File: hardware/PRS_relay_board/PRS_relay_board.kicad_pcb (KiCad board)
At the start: 2 copper layers, 28 parts, among them J1 691317410002, J2 691317410002, J3 691317410002, J4 691317410002, J5 UJ2-BH-2-TH, J6 530470610, J7 530470410, K1 T9AS1D12-5, K2 T9AS1D12-5, K3 T9AS1D12-5, K4 T9AS1D12-5, Q1 PMV37ENEA, Q2 PMV37ENEA, Q3 PMV37ENEA, Q4 PMV37ENEA

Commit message: Commit
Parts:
- removed J5: UJ2-BH-2-TH, UJ2-BH-2-TH:CUI_UJ2-BH-2-TH
- removed J6: 530470610, 530470610:MOLEX_530470610
- removed J7: 530470410, 530470410:MOLEX_530470410
- added C1: 100n, Capacitor_SMD:C_0603_1608Metric_Pad1.08x0.95mm_HandSolder, F.Cu at (234.0, -70.7)
- added C10: 100n, Capacitor_SMD:C_0603_1608Metric_Pad1.08x0.95mm_HandSolder, F.Cu at (224.9, -64.4)
- added C11: 100n, Capacitor_SMD:C_0603_1608Metric_Pad1.08x0.95mm_HandSolder, F.Cu at (229.7, -68.4)
- added C12: 100n, Capacitor_SMD:C_0603_1608Metric_Pad1.08x0.95mm_HandSolder, F.Cu at (223.7, -61.9)
- added C13: 10u, Capacitor_SMD:C_0805_2012Metric_Pad1.18x1.45mm_HandSolder, F.Cu at (131.0, 151.0)
- added C14: 100n, Capacitor_SMD:C_0603_1608Metric_Pad1.08x0.95mm_HandSolder, F.Cu at (241.7, -78.2)
- added C15: 100n, Capacitor_SMD:C_0603_1608Metric_Pad1.08x0.95mm_HandSolder, F.Cu at (219.4, -56.9)
- added C16: 100n, Capacitor_SMD:C_0603_1608Metric_Pad1.08x0.95mm_HandSolder, F.Cu at (237.1, -73.2)
- added C17: 1u, Capacitor_SMD:C_0603_1608Metric_Pad1.08x0.95mm_HandSolder, F.Cu at (229.7, -65.9)
- added C18: 100n, Capacitor_SMD:C_0603_1608Metric_Pad1.08x0.95mm_HandSolder, F.Cu at (246.5, -81.2)
- added C2: 100n, Capacitor_SMD:C_0603_1608Metric_Pad1.08x0.95mm_HandSolder, F.Cu at (248.9, -76.2)
- added C3: 10u, Capacitor_SMD:C_0805_2012Metric_Pad1.18x1.45mm_HandSolder, F.Cu at (237.6, -81.0)
- added C4: 100n, Capacitor_SMD:C_0603_1608Metric_Pad1.08x0.95mm_HandSolder, F.Cu at (231.5, -75.7)
- added C5: 100n, Capacitor_SMD:C_0603_1608Metric_Pad1.08x0.95mm_HandSolder, F.Cu at (237.4, -78.2)
- added C6: 100n, Capacitor_SMD:C_0603_1608Metric_Pad1.08x0.95mm_HandSolder, F.Cu at (219.4, -61.9)
- added C7: 100n, Capacitor_SMD:C_0603_1608Metric_Pad1.08x0.95mm_HandSolder, F.Cu at (232.8, -73.2)
- added C8: 100n, Capacitor_SMD:C_0603_1608Metric_Pad1.08x0.95mm_HandSolder, F.Cu at (242.2, -81.2)
- added C9: 100n, Capacitor_SMD:C_0603_1608Metric_Pad1.08x0.95mm_HandSolder, F.Cu at (235.8, -75.7)
- added FB1: Ferrite_Bead, Resistor_SMD:R_0603_1608Metric_Pad0.98x0.95mm_HandSolder, F.Cu at (223.7, -59.4)
- added H1: MountingHole, MountingHole:MountingHole_3.2mm_M3_DIN965, F.Cu at (78.0, 37.0)
- added H2: MountingHole, MountingHole:MountingHole_3.2mm_M3_DIN965, F.Cu at (151.0, 38.0)
- added IC1: USBLC6-4SC6, USBLC6-4SC6:SOT95P280X145-6N, F.Cu at (174.0, 39.0)
- added IC2: 74LVC125AD,118, 74LVC125AD,118:SOIC127P600X175-14N, F.Cu at (172.0, 129.0)
- added LED1: 553-0122F, 553-0122:5530122F, F.Cu at (55.0, 175.5)
- added LED2: 553-0122F, 553-0122:5530122F, F.Cu at (92.5, 175.5)
- added LED3: 553-0122F, 553-0122:5530122F, F.Cu at (130.0, 175.5)
- added LED4: 553-0122F, 553-0122:5530122F, F.Cu at (167.5, 175.5)
- added R10: 100k, Resistor_SMD:R_0603_1608Metric_Pad0.98x0.95mm_HandSolder, F.Cu at (232.4, -60.6)
- added R11: 100k, Resistor_SMD:R_0603_1608Metric_Pad0.98x0.95mm_HandSolder, F.Cu at (242.7, -70.7)
- added R12: 1k, Resistor_SMD:R_0603_1608Metric_Pad0.98x0.95mm_HandSolder, F.Cu at (228.1, -56.9)
- added R13: 1k, Resistor_SMD:R_0603_1608Metric_Pad0.98x0.95mm_HandSolder, F.Cu at (238.4, -68.2)
- added R14: 10k, Resistor_SMD:R_0603_1608Metric_Pad0.98x0.95mm_HandSolder, F.Cu at (245.5, -63.2)
- added R15: 10k, Resistor_SMD:R_0603_1608Metric_Pad0.98x0.95mm_HandSolder, F.Cu at (244.5, -75.7)
- added R16: 1k, Resistor_SMD:R_0603_1608Metric_Pad0.98x0.95mm_HandSolder, F.Cu at (228.1, -59.4)
- added R17: 1k, Resistor_SMD:R_0603_1608Metric_Pad0.98x0.95mm_HandSolder, F.Cu at (234.0, -65.7)
- added R18: 10k, Resistor_SMD:R_0603_1608Metric_Pad0.98x0.95mm_HandSolder, F.Cu at (241.5, -73.2)
- added R19: 10k, Resistor_SMD:R_0603_1608Metric_Pad0.98x0.95mm_HandSolder, F.Cu at (223.7, -56.9)
- added R20: 100R, Resistor_SMD:R_0603_1608Metric_Pad0.98x0.95mm_HandSolder, F.Cu at (238.4, -70.7)
- added R21: 100R, Resistor_SMD:R_0603_1608Metric_Pad0.98x0.95mm_HandSolder, F.Cu at (246.1, -78.7)
- added R22: 100R, Resistor_SMD:R_0603_1608Metric_Pad0.98x0.95mm_HandSolder, F.Cu at (234.0, -68.2)
- added R23: 100R, Resistor_SMD:R_0603_1608Metric_Pad0.98x0.95mm_HandSolder, F.Cu at (232.4, -63.1)
- added R24: 10k, Resistor_SMD:R_0603_1608Metric_Pad0.98x0.95mm_HandSolder, F.Cu at (236.8, -63.1)
- added R25: 1k, Resistor_SMD:R_0603_1608Metric_Pad0.98x0.95mm_HandSolder, F.Cu at (242.7, -68.2)
- added R26: 1k, Resistor_SMD:R_0603_1608Metric_Pad0.98x0.95mm_HandSolder, F.Cu at (232.4, -58.1)
- added R27: 10k, Resistor_SMD:R_0603_1608Metric_Pad0.98x0.95mm_HandSolder, F.Cu at (247.1, -70.7)
- added R28: 10k, Resistor_SMD:R_0603_1608Metric_Pad0.98x0.95mm_HandSolder, F.Cu at (236.8, -60.6)
- added R29: 330R, Resistor_SMD:R_0603_1608Metric_Pad0.98x0.95mm_HandSolder, F.Cu at (232.4, -55.6)
- added R30: 330R, Resistor_SMD:R_0603_1608Metric_Pad0.98x0.95mm_HandSolder, F.Cu at (242.7, -65.7)
- added R31: 330R, Resistor_SMD:R_0603_1608Metric_Pad0.98x0.95mm_HandSolder, F.Cu at (100.0, 172.5)
- added R32: 330R, Resistor_SMD:R_0603_1608Metric_Pad0.98x0.95mm_HandSolder, F.Cu at (100.0, 175.0)
- added R33: 330R, Resistor_SMD:R_0603_1608Metric_Pad0.98x0.95mm_HandSolder, F.Cu at (145.0, 207.5)
- added R34: 330R, Resistor_SMD:R_0603_1608Metric_Pad0.98x0.95mm_HandSolder, F.Cu at (145.0, 210.0)
- added R35: 330R, Resistor_SMD:R_0603_1608Metric_Pad0.98x0.95mm_HandSolder, F.Cu at (149.3, 207.5)
- added R36: 330R, Resistor_SMD:R_0603_1608Metric_Pad0.98x0.95mm_HandSolder, F.Cu at (149.3, 210.0)
- added R5: 1k, Resistor_SMD:R_0603_1608Metric_Pad0.98x0.95mm_HandSolder, F.Cu at (240.2, -75.7)
- added R6: 1k, Resistor_SMD:R_0603_1608Metric_Pad0.98x0.95mm_HandSolder, F.Cu at (228.1, -61.9)
- added R7: 10k, Resistor_SMD:R_0603_1608Metric_Pad0.98x0.95mm_HandSolder, F.Cu at (219.4, -59.4)
- added R8: 10k, Resistor_SMD:R_0603_1608Metric_Pad0.98x0.95mm_HandSolder, F.Cu at (238.4, -65.7)
- added R9: 100k, Resistor_SMD:R_0603_1608Metric_Pad0.98x0.95mm_HandSolder, F.Cu at (245.8, -73.2)
- added S1: 100SP1T2B4M7RE, 100SP1T2B4M7RE:100SP1T2B4M7RE, F.Cu at (35.0, 165.0)
- added S2: 100SP1T2B4M7RE, 100SP1T2B4M7RE:100SP1T2B4M7RE, F.Cu at (47.5, 165.0)
- added S3: 100SP1T2B4M7RE, 100SP1T2B4M7RE:100SP1T2B4M7RE, F.Cu at (72.5, 165.0)
- added S4: 100SP1T2B4M7RE, 100SP1T2B4M7RE:100SP1T2B4M7RE, F.Cu at (85.0, 165.0)
- added S5: 100SP1T2B4M7RE, 100SP1T2B4M7RE:100SP1T2B4M7RE, F.Cu at (110.0, 165.0)
- added S6: 100SP1T2B4M7RE, 100SP1T2B4M7RE:100SP1T2B4M7RE, F.Cu at (122.5, 165.0)
- added S7: 100SP1T2B4M7RE, 100SP1T2B4M7RE:100SP1T2B4M7RE, F.Cu at (147.5, 165.0)
- added S8: 100SP1T2B4M7RE, 100SP1T2B4M7RE:100SP1T2B4M7RE, F.Cu at (160.0, 165.0)
- added U1: MCP1825S-3302E/DB, Package_TO_SOT_SMD:SOT-223-3_TabPin2, F.Cu at (112.0, 145.0)
- added U2: STM32L052K6Tx, Package_QFP:LQFP-32_7x7mm_P0.8mm, F.Cu at (130.0, 141.0)
- J1, J2: value 691317410002 -> 691313410004; footprint 691317410002:691317410002 -> 691313410004:691313410004
- J3: value 691317410002 -> UJ2-BH-2-TH; footprint 691317410002:691317410002 -> UJ2-BH-2-TH:CUI_UJ2-BH-2-TH
- J4: value 691317410002 -> FTSH-105-01-F-DV-K-P; footprint 691317410002:691317410002 -> FTSH-105-01-F-DV-K:FTSH-105-XX-YYY-DV-K-P
- moved J4 113.6 mm to (155.0, 141.0), turned to 0 degrees
- moved D7 98.0 mm to (118.7, 101.6), turned to 270 degrees
- moved K3 90.4 mm to (91.8, 59.3), turned to 90 degrees
- moved D8 89.2 mm to (118.7, 94.0), turned to 270 degrees
- moved K4 87.1 mm to (130.2, 99.2), turned to 270 degrees
- moved D3 84.5 mm to (103.3, 56.9), turned to 90 degrees
- moved Q4 82.2 mm to (118.7, 87.7), turned to 270 degrees
- moved R4 78.2 mm to (118.7, 83.8), turned to 180 degrees
- moved D4 74.9 mm to (103.3, 64.7), turned to 90 degrees
- moved PS1 69.5 mm to (50.0, 119.0)
- moved Q3 67.7 mm to (103.3, 70.8), turned to 90 degrees
- moved R3 63.4 mm to (103.3, 74.6), turned to 0 degrees
- moved J1 53.4 mm to (65.0, 28.0), turned to 0 degrees
- moved D5 36.5 mm to (118.7, 70.7), turned to 270 degrees
- moved K1 35.4 mm to (91.8, 90.3), turned to 90 degrees
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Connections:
- J1 pad 1: Net-(J1-Pad1) -> /RELAY1_COM
- J1 pad 2: Net-(J1-Pad2) -> /RELAY1_NO
- J2 pad 1: Net-(J2-Pad1) -> /RELAY3_COM
- J2 pad 2: Net-(J2-Pad2) -> /RELAY3_NO
- J4 pad 1: Net-(J4-Pad1) -> +3V3
- J4 pad 2: Net-(J4-Pad2) -> /Sheet6168966E/SWDIO
- K1 pad 3: Net-(J1-Pad2) -> /RELAY1_COM
- K1 pad 4: Net-(J1-Pad1) -> /RELAY1_NO
- K2 pad 3: Net-(J2-Pad2) -> /RELAY3_COM
- K2 pad 4: Net-(J2-Pad1) -> /RELAY3_NO
- K3 pad 3: Net-(J3-Pad2) -> /RELAY2_COM
- K3 pad 4: Net-(J3-Pad1) -> /RELAY2_NO
- K4 pad 3: Net-(J4-Pad2) -> /RELAY4_COM
- K4 pad 4: Net-(J4-Pad1) -> /RELAY4_NO
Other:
- board outline added: 160 x 160 mm

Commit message: Commit
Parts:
- removed U1: MCP1825S-3302E/DB, Package_TO_SOT_SMD:SOT-223-3_TabPin2
- added C19: 100n, Capacitor_SMD:C_0603_1608Metric_Pad1.08x0.95mm_HandSolder, F.Cu at (233.2, 138.3)
- added D9: MMBD7000HC, Package_TO_SOT_SMD:SOT-23_Handsoldering, F.Cu at (161.0, 129.0)
- added H3: MountingHole, MountingHole:MountingHole_3.2mm_M3_DIN965, F.Cu at (65.0, 180.0)
- added H4: MountingHole, MountingHole:MountingHole_3.2mm_M3_DIN965, F.Cu at (215.0, 180.0)
- added IC3: STCN75, STCN75:SOP65P490X110-8N, F.Cu at (145.0, 135.0)
- added IC4: UA78M33CKVURG3, UA78M33CKVURG3:TPS7A6533QKVURQ1, F.Cu at (139.0, 126.0)
- added J5: 10-32-1031, 10-32-1031:SHDR3W114P0X508_1X3_1416X1140X1425P, F.Cu at (68.0, 129.0)
- added Q5: BC848, Package_TO_SOT_SMD:SOT-23_Handsoldering, F.Cu at (163.0, 118.0)
- added Q6: PMV37ENEA, Package_TO_SOT_SMD:SOT-23_Handsoldering, F.Cu at (167.4, 129.0)
- added R37: R, Resistor_SMD:R_0603_1608Metric_Pad0.98x0.95mm_HandSolder, F.Cu at (237.6, 138.3)
- added R38: R, Resistor_SMD:R_0603_1608Metric_Pad0.98x0.95mm_HandSolder, F.Cu at (201.4, 146.7)
- added R39: 100R, Resistor_SMD:R_0603_1608Metric_Pad0.98x0.95mm_HandSolder, F.Cu at (196.6, 129.7)
- added R40: 10k, Resistor_SMD:R_0603_1608Metric_Pad0.98x0.95mm_HandSolder, F.Cu at (168.4, 117.0)
- added R41: 1k, Resistor_SMD:R_0603_1608Metric_Pad0.98x0.95mm_HandSolder, F.Cu at (168.4, 119.5)
- added R42: 10k, Resistor_SMD:R_0603_1608Metric_Pad0.98x0.95mm_HandSolder, F.Cu at (159.9, 132.5)
- added R43: R, Resistor_SMD:R_0603_1608Metric_Pad0.98x0.95mm_HandSolder, F.Cu at (211.0, 81.0)
- added R44: R, Resistor_SMD:R_0603_1608Metric_Pad0.98x0.95mm_HandSolder, F.Cu at (211.0, 83.5)
- C3: value 10u -> 330n; footprint Capacitor_SMD:C_0805_2012Metric_Pad1.18x1.45mm_HandSolder -> Capacitor_SMD:C_0603_1608Metric_Pad1.08x0.95mm_HandSolder
- IC1: value USBLC6-4SC6 -> USBLC6-2SC6
- K1, K2, K3, K4: value T9AS1D12-5 -> 1-1393210-3; footprint T9AS1D12-5:T9AS1D125 -> T9AS1D12-12:TE_1-1393210-3
- PS1: value RAC10-05SK_277 -> RAC10-12SK_277; footprint RAC10-05SK_277:RAC1005SK277 -> RAC10-12SK_277:RAC10-12SK_277
- R9: value 100k -> R
- moved R5 290.4 mm to (78.0, 165.2), turned to 180 degrees
- moved C2 287.4 mm to (90.6, 163.6), turned to 180 degrees
- moved R30 281.8 mm to (93.0, 173.0), turned to 90 degrees
- moved C1 281.5 mm to (78.0, 163.6), turned to 180 degrees
- moved R8 275.5 mm to (90.6, 166.8)
- moved R15 269.9 mm to (126.0, 166.8)
- moved R7 266.7 mm to (78.0, 166.8)
- moved R29 266.4 mm to (95.6, 173.0), turned to 90 degrees
- moved R6 265.5 mm to (90.6, 165.2), turned to 180 degrees
- moved R14 265.1 mm to (113.6, 166.8)
- moved C7 259.8 mm to (126.0, 163.6), turned to 180 degrees
- moved R13 259.0 mm to (126.0, 165.2), turned to 180 degrees
- moved R18 256.9 mm to (150.0, 166.8)
- moved C9 254.2 mm to (150.0, 163.6), turned to 180 degrees
- moved R12 249.9 mm to (113.6, 165.2), turned to 180 degrees
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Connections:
- C3 pad 1: +5V -> +12V
- D1 pad 2: +5V -> +12V
- D3 pad 2: +5V -> +12V
- D5 pad 2: +5V -> +12V
- D7 pad 2: +5V -> +12V
- IC1 pad 1: /Sheet6168966E/USB_D- -> /Sheet6168966E/EXT_USB_D-
- IC1 pad 3: /Sheet6168966E/USB_D+ -> /Sheet6168966E/EXT_USB_D+
- IC1 pad 4: /Sheet6168966E/ID -> /Sheet6168966E/USB_D+
- IC1 pad 6: Net-(IC1-Pad6) -> /Sheet6168966E/USB_D-
- IC2 pad 1: /Sheet6168966E/~1OE -> GND
- IC2 pad 10: /Sheet6168966E/~3OE -> GND
- IC2 pad 13: /Sheet6168966E/~4OE -> GND
- IC2 pad 4: /Sheet6168966E/~2OE -> GND
- J3 pad 1: Net-(J3-Pad1) -> /Sheet6168966E/VBUS
- J3 pad 2: Net-(J3-Pad2) -> /Sheet6168966E/EXT_USB_D-
- J3 pad 3: Net-(J3-Pad3) -> /Sheet6168966E/EXT_USB_D+
- J3 pad 4: Net-(J3-Pad4) -> GND
- PS1 pad 5: +5V -> +12V
- R9 pad 1: /Sheet6168966E/ID -> +3V3
- R9 pad 2: GND -> /Sheet6168966E/SDA
- U2 pad 14: Net-(U2-Pad14) -> Net-(R23-Pad1)
- U2 pad 15: Net-(U2-Pad15) -> Net-(R22-Pad1)
- U2 pad 18: Net-(U2-Pad18) -> Net-(R21-Pad1)
- U2 pad 19: Net-(U2-Pad19) -> Net-(R20-Pad1)
- U2 pad 27: Net-(R20-Pad1) -> /Sheet6168966E/FAN_TACH
- U2 pad 28: Net-(R21-Pad1) -> /Sheet6168966E/TEMP_INT
- U2 pad 29: Net-(R22-Pad1) -> /Sheet6168966E/SCL
- U2 pad 30: Net-(R23-Pad1) -> /Sheet6168966E/SDA
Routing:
- net /Sheet6168966E/1Y: track 0.00 -> 95.1 mm
- net /Sheet6168966E/2Y: track 0.00 -> 54.6 mm
- net /Sheet6168966E/4Y: track 0.00 -> 44.6 mm
- net GND: track 0.00 -> 40.9 mm
- net /Sheet6168966E/3Y: track 0.00 -> 27.5 mm
- net Net-(LED3-Pad2): track 0.00 -> 6.77 mm
- net Net-(LED1-Pad2): track 0.00 -> 6.77 mm
- net Net-(LED4-Pad2): track 0.00 -> 6.73 mm
- net Net-(LED2-Pad2): track 0.00 -> 6.73 mm
- net /Sheet6168966E/RELAY2_IN: track 0.00 -> 6.68 mm
- net Net-(R25-Pad2): track 0.00 -> 4.19 mm
- net Net-(R17-Pad2): track 0.00 -> 4.19 mm
- net Net-(R6-Pad2): track 0.00 -> 4.19 mm
- net Net-(R12-Pad2): track 0.00 -> 4.19 mm
- net Net-(R5-Pad2): track 0.00 -> 4.09 mm
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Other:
- board size 160 x 160 mm -> 160 x 135 mm
- copper layers 2 -> 4

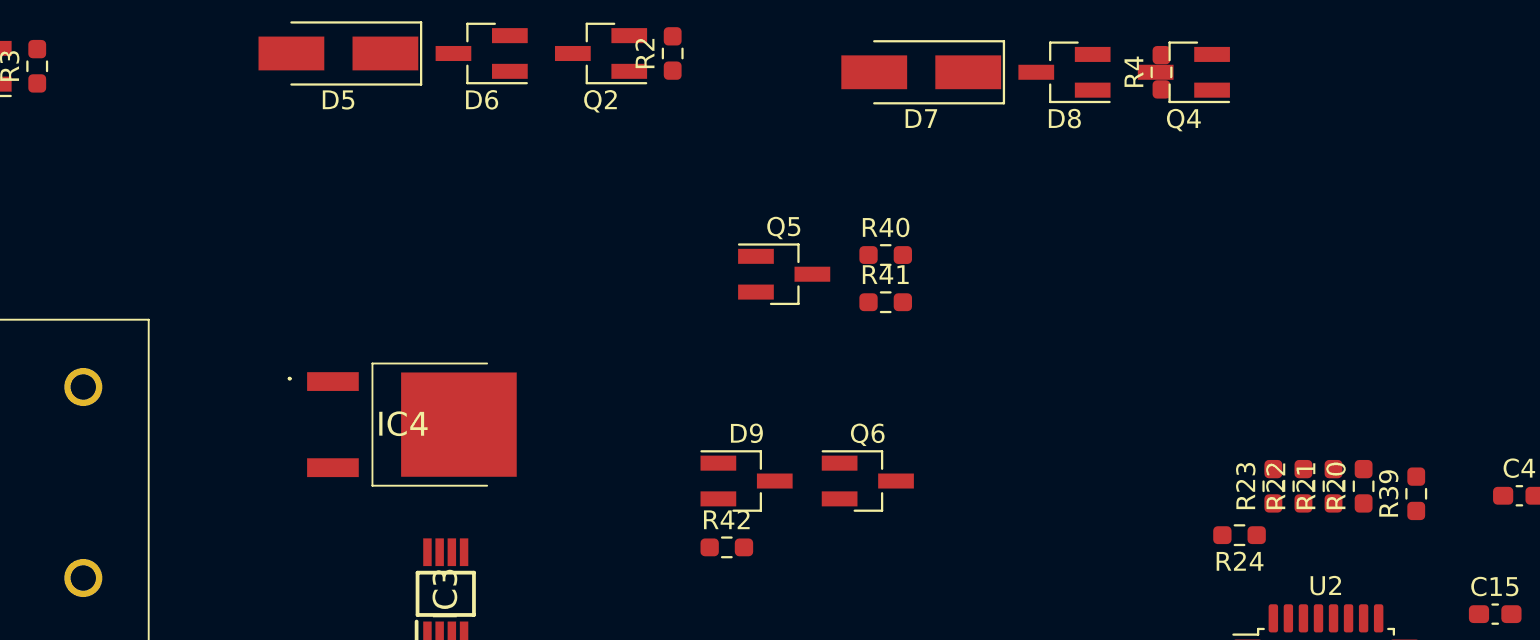
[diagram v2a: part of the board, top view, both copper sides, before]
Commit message: Add Fan connector
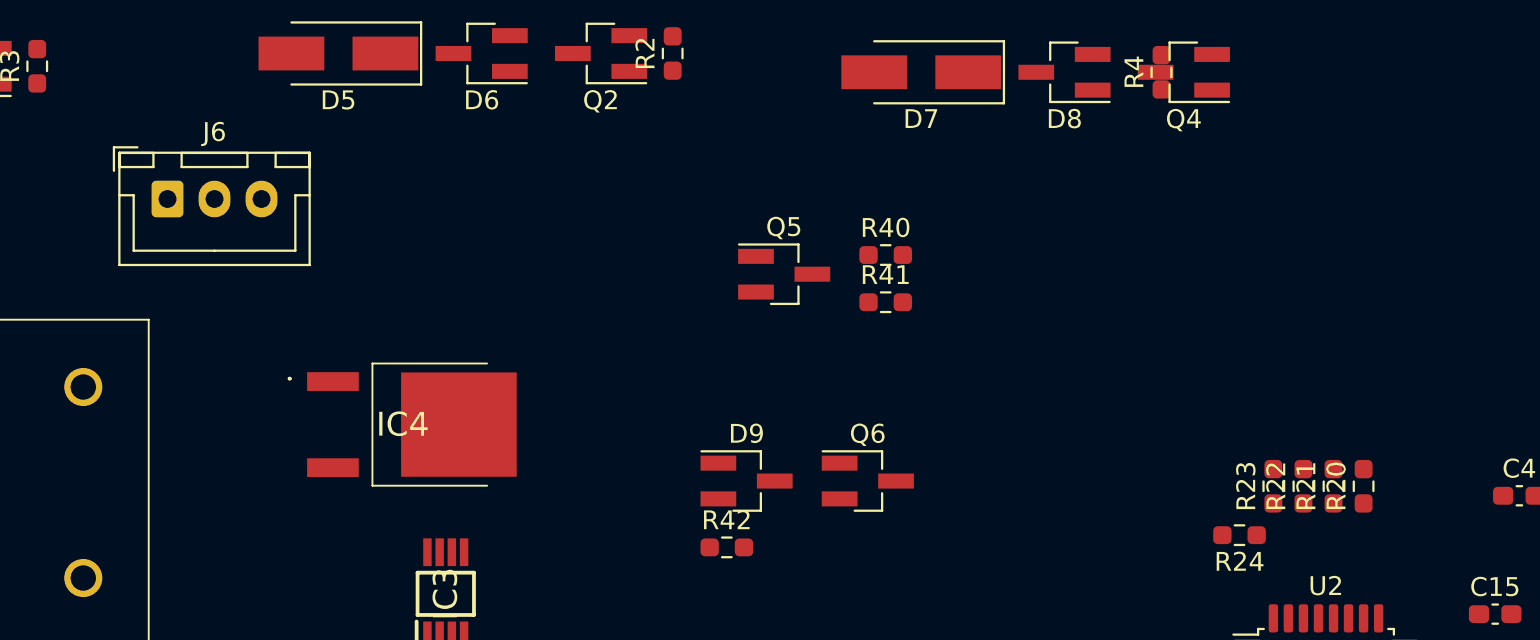
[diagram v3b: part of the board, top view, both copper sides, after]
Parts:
- removed R39: 100R, Resistor_SMD:R_0603_1608Metric_Pad0.98x0.95mm_HandSolder
- added J6: B3B-XH-A, Connector_JST:JST_XH_B3B-XH-A_1x03_P2.50mm_Vertical, F.Cu at (130.2, 114.0)
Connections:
- U2 pad 26: Net-(R39-Pad1) -> /Sheet6168966E/FAN_CTRL

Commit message: Add BOM
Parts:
- removed IC2: 74LVC125AD,118, 74LVC125AD,118:SOIC127P600X175-14N
- removed IC3: STCN75, STCN75:SOP65P490X110-8N
- removed IC4: UA78M33CKVURG3, UA78M33CKVURG3:TPS7A6533QKVURQ1
- removed R44: R, Resistor_SMD:R_0603_1608Metric_Pad0.98x0.95mm_HandSolder
- added R39: 10k, Resistor_SMD:R_0603_1608Metric_Pad0.98x0.95mm_HandSolder, F.Cu at (343.4, 141.3)
- added U1: STCN75, STCN75:SOP65P490X110-8N, F.Cu at (326.7, 143.1)
- added U3: 74LVC125AD,118, 74LVC125AD,118:SOIC127P600X175-14N, F.Cu at (307.9, 150.6)
- added U5: UA78M33CKVURG3, UA78M33CKVURG3:TPS7A6533QKVURQ1, F.Cu at (356.7, 97.4)
- D1, D3, D5, D7: value D_Zener -> MM3Z24VST1G; footprint Diode_SMD:D_SMA_Handsoldering -> Diode_SMD:D_SOD-323
- FB1: value Ferrite_Bead -> BLM18HE601SN1D
- R12, R41: value 1k -> 10k
- R13, R25, R26, R5: value 1k -> 330R
- R14, R15, R27: value 10k -> 330R
- R28, R40, R7: value 10k -> 1k
- R29, R33, R34: value 330R -> 1k
- R30, R31, R35, R36: value 330R -> 10k
- R37, R38, R9: value R -> 10k
- R42: value 10k -> R
- U2: value STM32L052K6Tx -> STM32L062K8Tx
- moved J5 347.8 mm to (410.8, 70.0), turned to 0 degrees
- moved PS1 283.4 mm to (357.7, 67.7)
- moved K2 248.8 mm to (326.8, 89.3)
- moved R6 224.5 mm to (314.3, 146.7), turned to 0 degrees
- moved LED1 214.2 mm to (306.1, 138.2)
- moved C5 208.2 mm to (410.2, 77.6)
- moved J6 197.5 mm to (326.4, 136.3)
- moved C2 195.3 mm to (285.4, 178.0), turned to 0 degrees
- moved Q1 194.9 mm to (284.3, 104.0), turned to 0 degrees
- moved D2 194.8 mm to (277.8, 108.5), turned to 0 degrees
- moved R5 194.7 mm to (272.3, 178.0), turned to 0 degrees
- moved D1 194.1 mm to (269.6, 108.5), turned to 0 degrees
- moved R8 190.7 mm to (281.0, 178.0)
- moved R7 190.3 mm to (267.9, 178.0)
- moved D9 183.7 mm to (344.6, 135.2)
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- renumbered IC1 to U4
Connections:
- net /RELAY1_COM renamed /Relays/RELAY1_COM
- net /RELAY1_NO renamed /Relays/RELAY1_NO
- net /RELAY2_COM renamed /Relays/RELAY2_COM
- net /RELAY2_NO renamed /Relays/RELAY2_NO
- net /RELAY3_COM renamed /Relays/RELAY3_COM
- net /RELAY3_NO renamed /Relays/RELAY3_NO
- net /RELAY4_COM renamed /Relays/RELAY4_COM
- net /RELAY4_NO renamed /Relays/RELAY4_NO
- net /Sheet6168966E/EXT_USB_D+ renamed /MCU/EXT_USB_D+
- net /Sheet6168966E/EXT_USB_D- renamed /MCU/EXT_USB_D-
- net /Sheet6168966E/SCL renamed /Cooling/SCL
- net /Sheet6168966E/SDA renamed /Cooling/SDA
- net /Sheet6168966E/SWCLK renamed /MCU/SWCLK
- net /Sheet6168966E/SWDIO renamed /MCU/SWDIO
- net /Sheet6168966E/USB_D+ renamed /MCU/USB_D+
- net /Sheet6168966E/USB_D- renamed /MCU/USB_D-
- net /Sheet6168966E/VBUS renamed /MCU/VBUS
- net /Sheet6168966E/VBUS_SENSE renamed /MCU/VBUS_SENSE
- net /Sheet6168966E/VDDA renamed /MCU/VDDA
- net /Sheet6168966E/~RST renamed /MCU/~RST
- C1 pad 1: /Sheet6168966E/RELAY1_USB_MAN -> /Front Panel/RELAY1_USB_MAN
- C10 pad 1: /Sheet6168966E/RELAY3_IN -> /Front Panel/RELAY3_USB_MAN
- C11 pad 1: /Sheet6168966E/RELAY4_USB_MAN -> /Front Panel/RELAY3_IN
- C12 pad 1: /Sheet6168966E/RELAY4_IN -> /Front Panel/RELAY4_USB_MAN
- C16 pad 1: +3V3 -> /Front Panel/RELAY4_IN
- C2 pad 1: /Sheet6168966E/RELAY1_IN -> /Front Panel/RELAY1_IN
- C6 pad 1: /Sheet6168966E/RELAY2_USB_MAN -> +3V3
- C7 pad 1: /Sheet6168966E/RELAY2_IN -> /Front Panel/RELAY2_USB_MAN
- C9 pad 1: /Sheet6168966E/RELAY3_USB_MAN -> /Front Panel/RELAY2_IN
- K1 pad A2: Net-(D4-Pad1) -> Net-(D6-Pad1)
- K4 pad A2: Net-(D6-Pad1) -> Net-(D4-Pad1)
- Q1 pad 1: /RELAY1_OUT -> /Front Panel/RELAY3_OUT
- Q1 pad 3: Net-(D2-Pad1) -> Net-(D6-Pad1)
- Q2 pad 1: /RELAY2_OUT -> /Front Panel/RELAY1_OUT
- Q2 pad 3: Net-(D6-Pad1) -> Net-(D2-Pad1)
- Q3 pad 1: /RELAY3_OUT -> /Front Panel/RELAY4_OUT
- Q3 pad 3: Net-(D4-Pad1) -> Net-(D8-Pad1)
- Q4 pad 1: /RELAY4_OUT -> /Front Panel/RELAY2_OUT
- Q4 pad 3: Net-(D8-Pad1) -> Net-(D4-Pad1)
- R1 pad 1: /RELAY1_OUT -> /Front Panel/RELAY1_OUT
- R12 pad 1: /Sheet6168966E/RELAY2_USB_MAN -> +3V3
- R12 pad 2: Net-(R12-Pad2) -> /Front Panel/RELAY1_IN
- R13 pad 1: /Sheet6168966E/RELAY2_IN -> Net-(LED1-Pad2)
- R13 pad 2: Net-(R13-Pad2) -> /Front Panel/1Y
- R14 pad 1: +3V3 -> Net-(LED2-Pad3)
- R14 pad 2: /Sheet6168966E/RELAY2_USB_MAN -> /Front Panel/2Y
- R15 pad 1: +3V3 -> Net-(LED2-Pad2)
- R15 pad 2: /Sheet6168966E/RELAY2_IN -> /Front Panel/2Y
- R16 pad 1: /Sheet6168966E/RELAY3_USB_MAN -> /Front Panel/RELAY2_USB_MAN
- R17 pad 1: /Sheet6168966E/RELAY3_IN -> /Front Panel/RELAY2_IN
- R18 pad 2: /Sheet6168966E/RELAY3_USB_MAN -> /Front Panel/RELAY2_USB_MAN
- R19 pad 2: /Sheet6168966E/RELAY3_IN -> /Front Panel/RELAY2_IN
- R2 pad 1: /RELAY2_OUT -> /Front Panel/RELAY2_OUT
- R20 pad 2: /Sheet6168966E/RELAY4_OUT -> /Front Panel/RELAY4_OUT
- R21 pad 2: /Sheet6168966E/RELAY3_OUT -> /Front Panel/RELAY3_OUT
- R22 pad 2: /Sheet6168966E/RELAY2_OUT -> /Front Panel/RELAY2_OUT
- R23 pad 2: /Sheet6168966E/RELAY1_OUT -> /Front Panel/RELAY1_OUT
- R25 pad 1: /Sheet6168966E/RELAY4_USB_MAN -> Net-(LED3-Pad3)
- R25 pad 2: Net-(R25-Pad2) -> /Front Panel/3Y
- R26 pad 1: /Sheet6168966E/RELAY4_IN -> /Front Panel/3Y
- R26 pad 2: Net-(R26-Pad2) -> Net-(LED3-Pad2)
- R27 pad 1: +3V3 -> Net-(LED4-Pad3)
- R27 pad 2: /Sheet6168966E/RELAY4_USB_MAN -> /Front Panel/4Y
- R28 pad 1: +3V3 -> /Front Panel/RELAY3_USB_MAN
- R28 pad 2: /Sheet6168966E/RELAY4_IN -> Net-(R28-Pad2)
- R29 pad 1: Net-(LED1-Pad2) -> /Front Panel/RELAY3_IN
- R29 pad 2: /Sheet6168966E/1Y -> Net-(R29-Pad2)
- R3 pad 1: /RELAY3_OUT -> /Front Panel/RELAY3_OUT
- R30 pad 1: Net-(LED1-Pad3) -> +3V3
- R30 pad 2: /Sheet6168966E/1Y -> /Front Panel/RELAY3_USB_MAN
- R31 pad 1: Net-(LED2-Pad3) -> +3V3
- R31 pad 2: /Sheet6168966E/2Y -> /Front Panel/RELAY3_IN
- R32 pad 1: Net-(LED2-Pad2) -> /Front Panel/4Y
- R32 pad 2: /Sheet6168966E/2Y -> Net-(LED4-Pad2)
- R33 pad 1: Net-(LED3-Pad3) -> /Front Panel/RELAY4_USB_MAN
- R33 pad 2: /Sheet6168966E/3Y -> Net-(R33-Pad2)
- R34 pad 1: Net-(LED4-Pad3) -> /Front Panel/RELAY4_IN
- R34 pad 2: /Sheet6168966E/4Y -> Net-(R34-Pad2)
- R35 pad 1: /Sheet6168966E/3Y -> +3V3
- R35 pad 2: Net-(LED3-Pad2) -> /Front Panel/RELAY4_USB_MAN
- R36 pad 1: /Sheet6168966E/4Y -> +3V3
- R36 pad 2: Net-(LED4-Pad2) -> /Front Panel/RELAY4_IN
- R38 pad 2: /Sheet6168966E/INT -> /Cooling/TEMP_INT
- R4 pad 1: /RELAY4_OUT -> /Front Panel/RELAY4_OUT
- R40 pad 1: Net-(Q5-Pad1) -> +12V
- R40 pad 2: /FAN_CTRL -> Net-(Q5-Pad3)
- R41 pad 1: +12V -> Net-(Q5-Pad3)
- R41 pad 2: Net-(Q5-Pad3) -> GND
- R42 pad 1: Net-(Q5-Pad3) -> Net-(J6-Pad2)
- R42 pad 2: GND -> /Cooling/FAN_TACH
- R43 pad 1: Net-(J6-Pad2) -> /Cooling/FAN_TACH
- R43 pad 2: /FAN_TACH -> GND
- R5 pad 1: /Sheet6168966E/RELAY1_USB_MAN -> Net-(LED1-Pad3)
- R5 pad 2: Net-(R5-Pad2) -> /Front Panel/1Y
- R6 pad 1: /Sheet6168966E/RELAY1_IN -> /Front Panel/RELAY1_USB_MAN
- R7 pad 1: +3V3 -> /Front Panel/RELAY1_IN
- R7 pad 2: /Sheet6168966E/RELAY1_USB_MAN -> Net-(R7-Pad2)
- R8 pad 2: /Sheet6168966E/RELAY1_IN -> /Front Panel/RELAY1_USB_MAN
- S1 pad 2: Net-(R5-Pad2) -> Net-(R6-Pad2)
- S2 pad 2: Net-(R6-Pad2) -> Net-(R7-Pad2)
- S3 pad 2: Net-(R12-Pad2) -> Net-(R16-Pad2)
- S4 pad 2: Net-(R13-Pad2) -> Net-(R17-Pad2)
- S5 pad 2: Net-(R16-Pad2) -> Net-(R28-Pad2)
- S6 pad 2: Net-(R17-Pad2) -> Net-(R29-Pad2)
- S7 pad 2: Net-(R25-Pad2) -> Net-(R33-Pad2)
- S8 pad 2: Net-(R26-Pad2) -> Net-(R34-Pad2)
- U2 pad 10: /Sheet6168966E/RELAY3_IN -> /Front Panel/RELAY3_IN
- U2 pad 11: /Sheet6168966E/RELAY3_USB_MAN -> /Front Panel/RELAY3_USB_MAN
- U2 pad 12: /Sheet6168966E/RELAY4_IN -> /Front Panel/RELAY4_IN
- U2 pad 13: /Sheet6168966E/RELAY4_USB_MAN -> /Front Panel/RELAY4_USB_MAN
- U2 pad 26: /Sheet6168966E/FAN_CTRL -> /Cooling/FAN_CTRL
- U2 pad 27: /Sheet6168966E/FAN_TACH -> /Cooling/FAN_TACH
- U2 pad 28: /Sheet6168966E/TEMP_INT -> /Cooling/TEMP_INT
- U2 pad 6: /Sheet6168966E/RELAY1_IN -> /Front Panel/RELAY1_IN
- U2 pad 7: /Sheet6168966E/RELAY1_USB_MAN -> /Front Panel/RELAY1_USB_MAN
- U2 pad 8: /Sheet6168966E/RELAY2_IN -> /Front Panel/RELAY2_IN
- U2 pad 9: /Sheet6168966E/RELAY2_USB_MAN -> /Front Panel/RELAY2_USB_MAN
